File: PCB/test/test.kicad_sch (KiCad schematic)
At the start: 56 parts, among them CN4 HEADER_1X4, CN5 UFL, SW2 MLL1200S_TE, U1 STM32WBxx_QFN48, U2 USBLC6-2SC6, U3 LD3985M33R, X1 NX2016_32MHz, X2 NX2012_32K768Hz

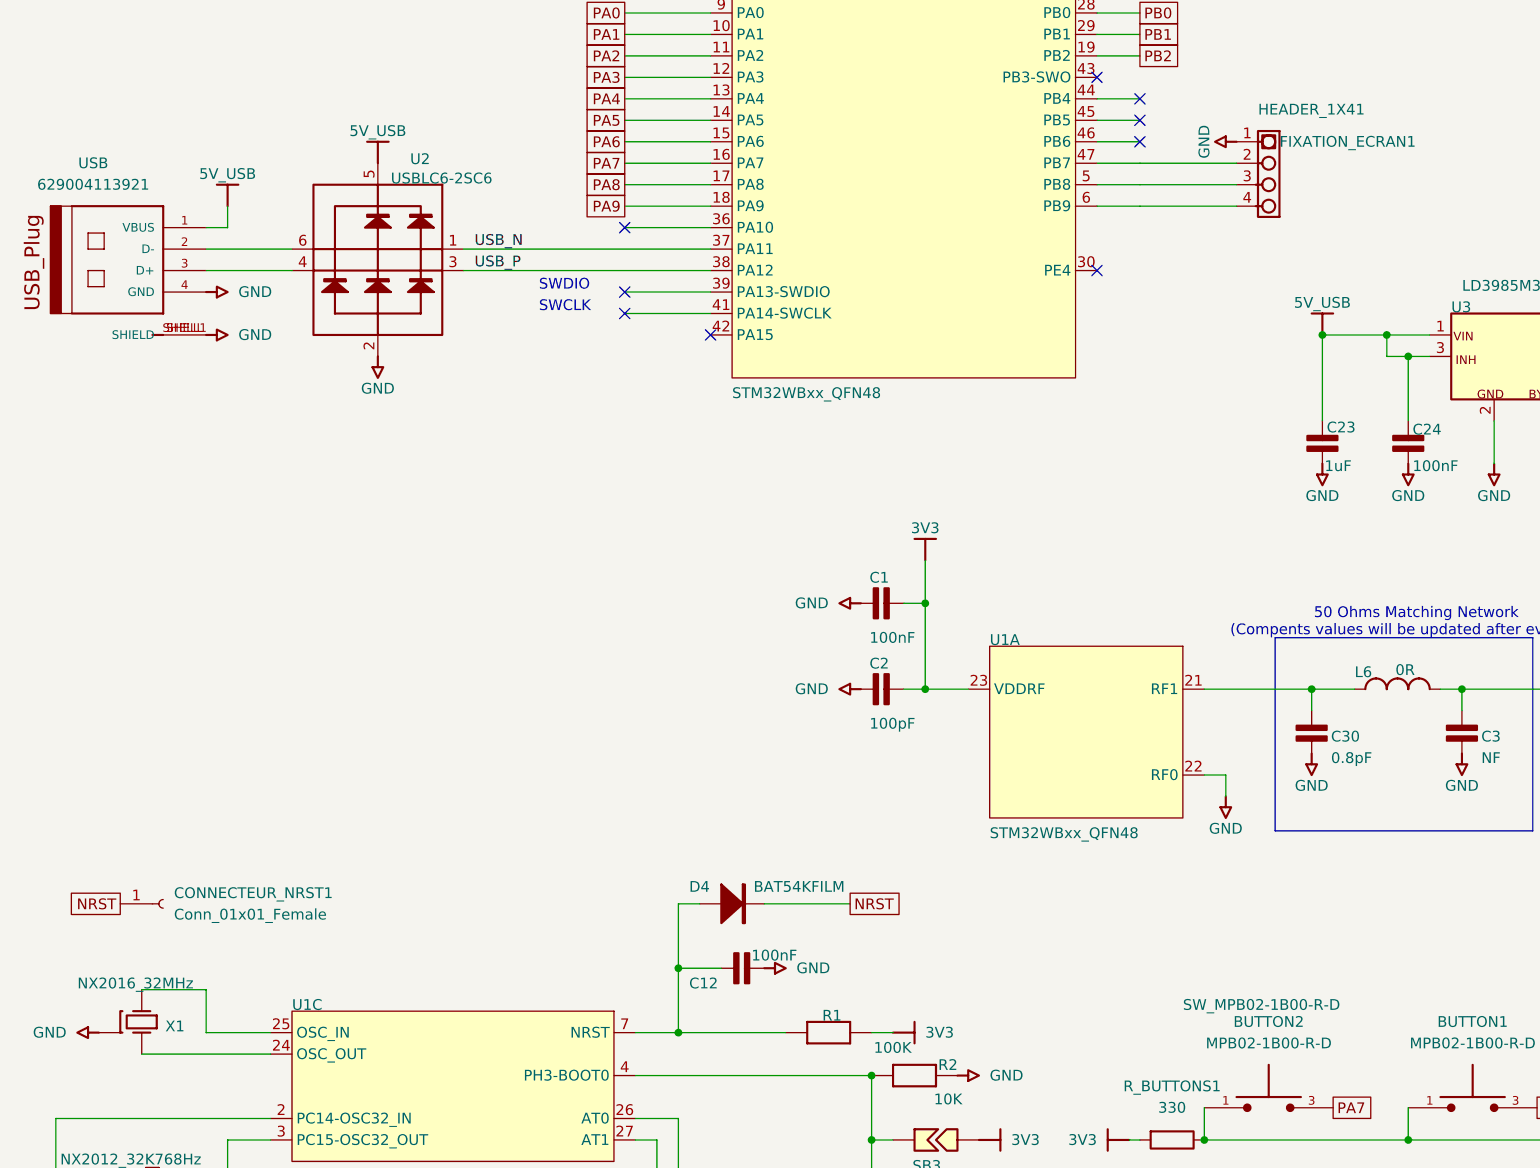
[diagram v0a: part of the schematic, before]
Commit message: ajout de l'usb dans le pcb
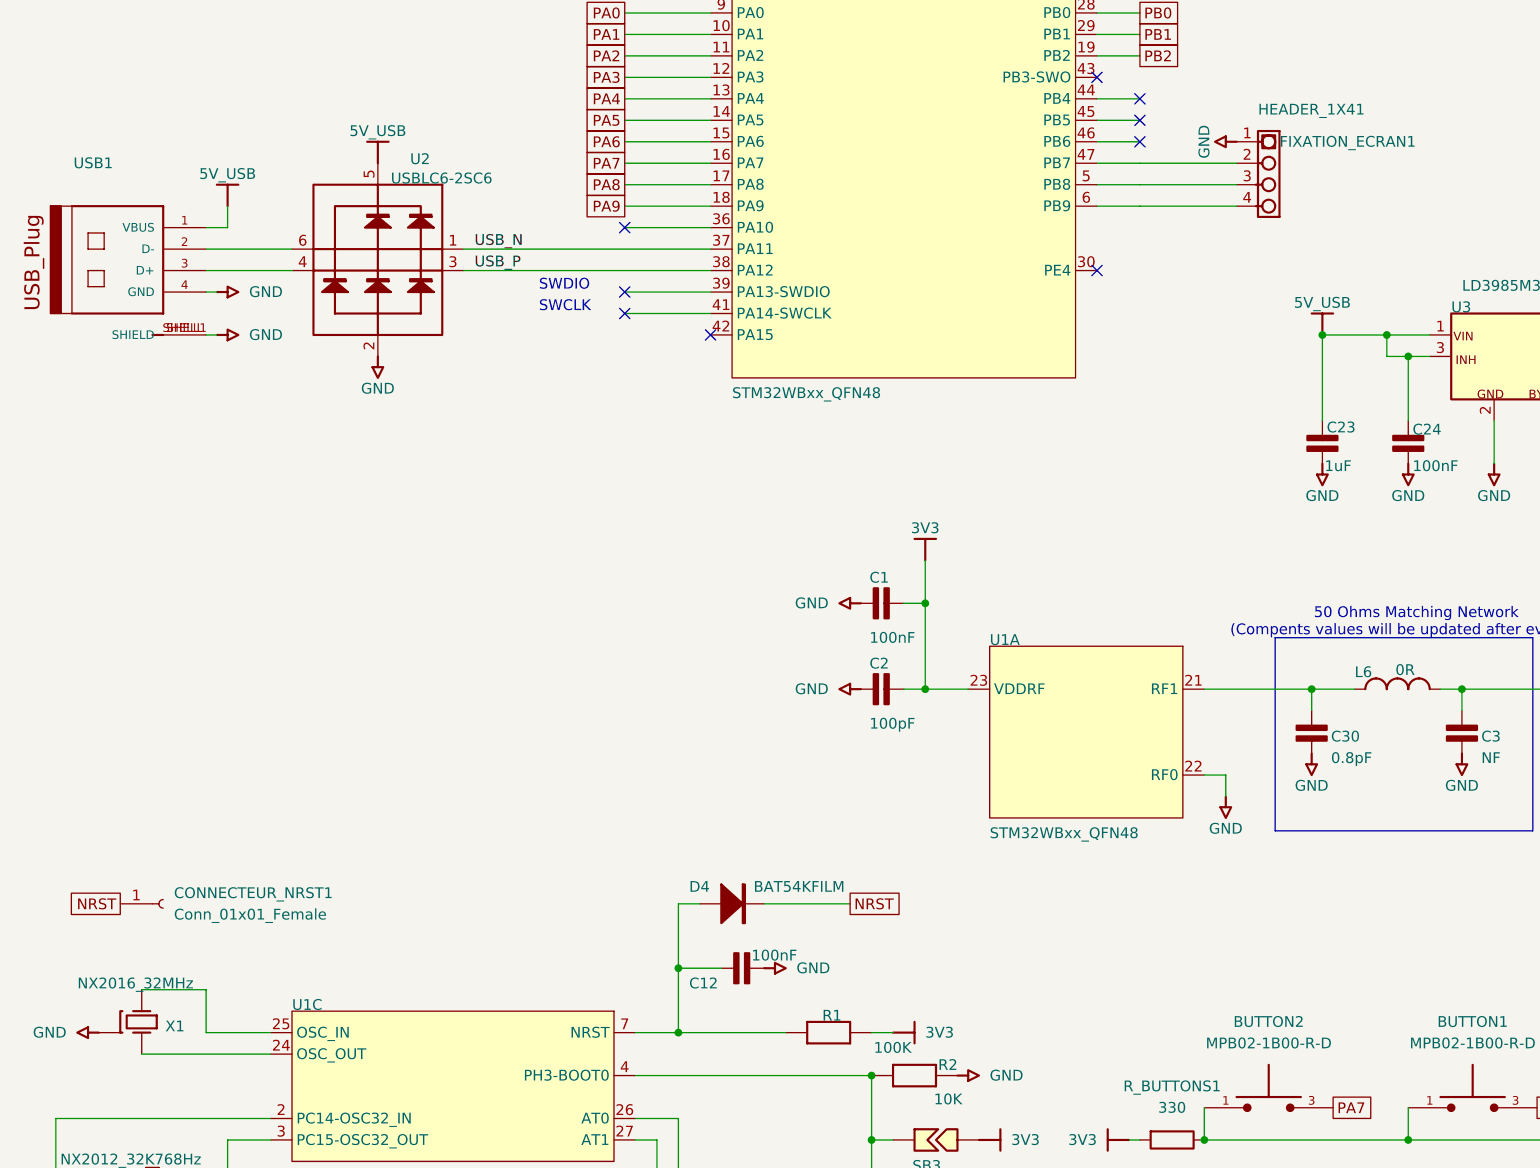
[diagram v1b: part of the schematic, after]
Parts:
- BUTTON1, BUTTON2, BUTTON3: footprint SW_MPB02-1B00-R-D -> (none)
- BUZZER1: footprint CUI_CMT-4023S-SMT-TR -> (none)
- C1, C10, C12, C15, C16, C17, C18, C19, C2, C20, C21, C22, C24, C25, C27, C28, C29, C3, C30, C4, C6, C7, C8, C9: footprint 0402_CAP_NPOL -> (none)
- C23, C26: footprint 0603_CAP_NPOL -> (none)
- CN4: footprint SIL4_127_B -> (none)
- CN5: footprint UFL -> (none)
- D4: footprint SOD523 -> (none)
- FLT1: footprint LFB182G45CGFD436 -> (none)
- L1, L4, L6: footprint 0402_COIL -> (none)
- L2: footprint 0805_COIL -> (none)
- L3: footprint 0603_COIL -> (none)
- OXYMETER1: footprint XDCR_SFH_7060 -> (none)
- R1, R2: footprint 0402_RES -> (none)
- SB1, SB3, SB4, SB5: footprint SB-tiny -> (none)
- SW2: footprint MLL1200S_TE -> (none)
- U1: footprint STM32WBxx_QFN48 -> (none)
- U2: footprint SOT23-6 -> (none)
- U3: footprint SOT23-5 -> (none)
- USB1: renamed from USB; value 629004113921 -> (none); footprint 629004113921 -> (none)
- X1: footprint NX2016_4P -> (none)
- X2: footprint NX2012_2P -> (none)

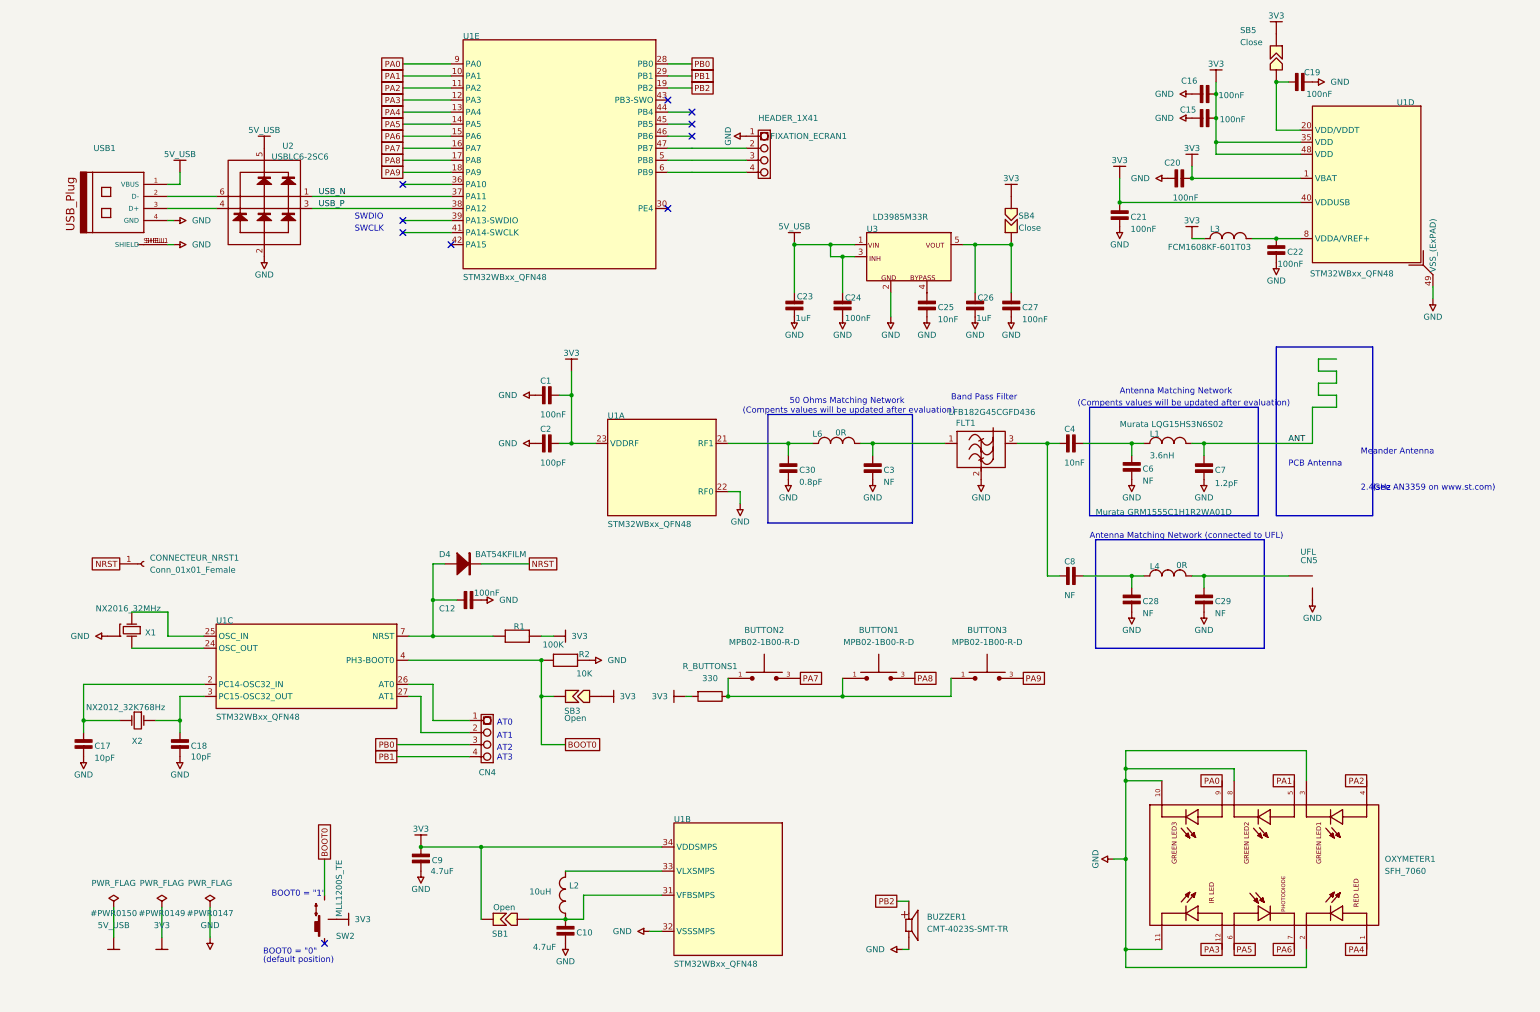
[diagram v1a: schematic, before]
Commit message: nouveaux boutons, réduction taille
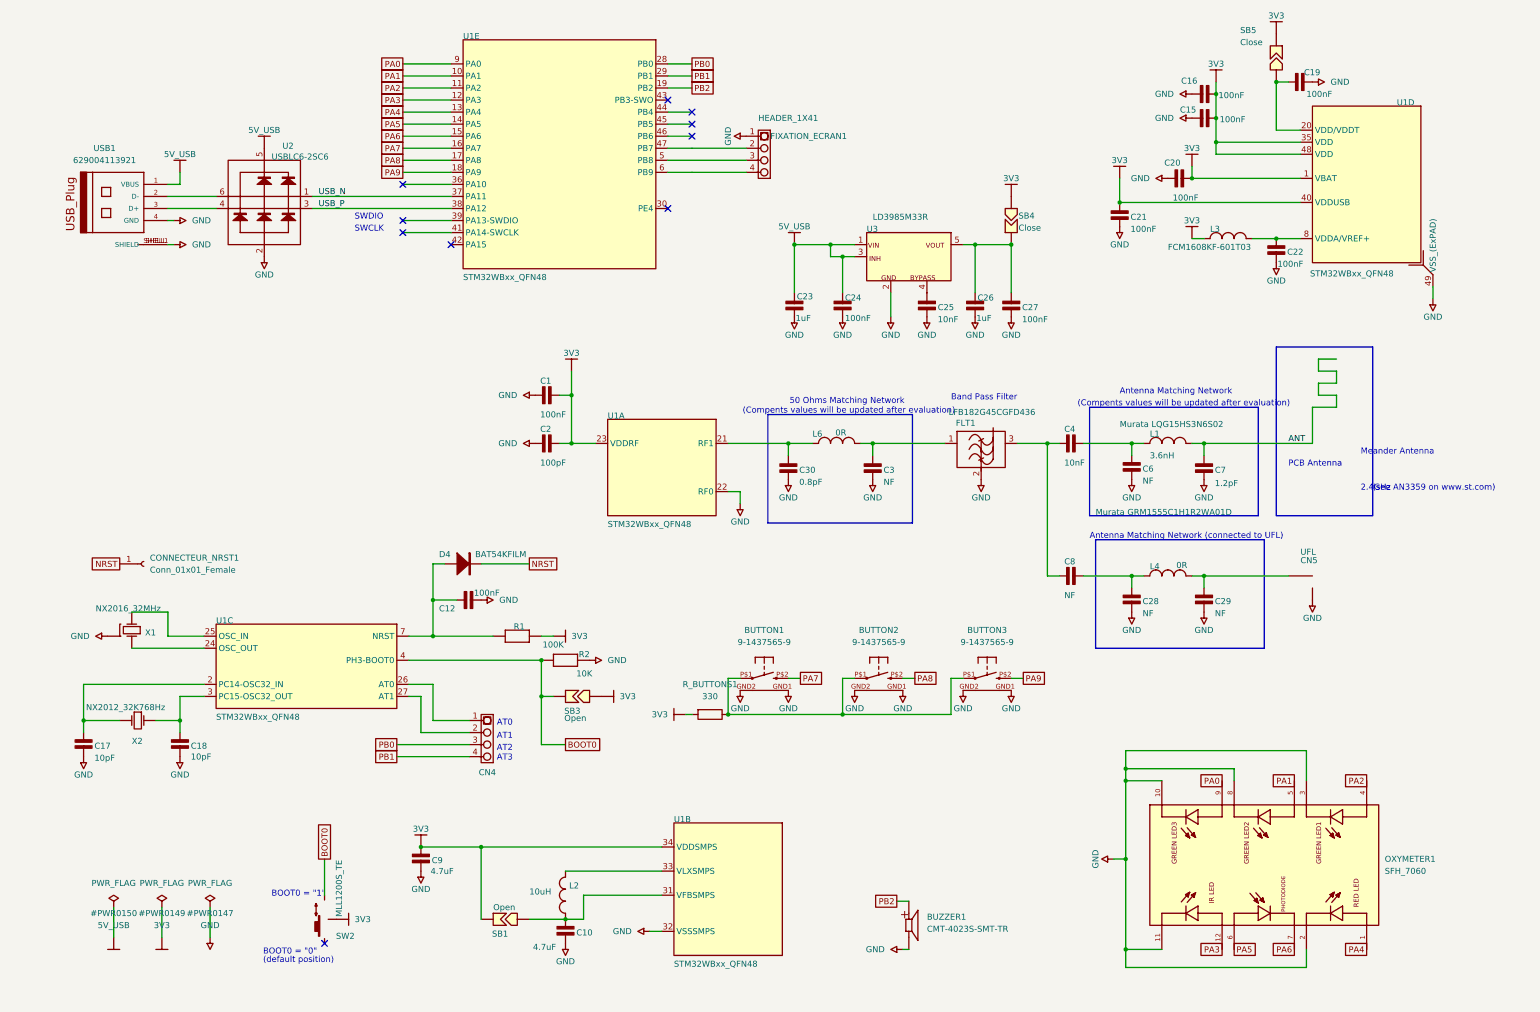
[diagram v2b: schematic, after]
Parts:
- removed BUTTON1, BUTTON2, BUTTON3: MPB02-1B00-R-D, symbol MPB02-1B00-R-D:MPB02-1B00-R-D
- added BUTTON1, BUTTON2, BUTTON3: 9-1437565-9, FSMRACD, symbol 9-1437565-9:9-1437565-9
- BUZZER1: footprint (none) -> CMT-4023S-SMT-TR:CUI_CMT-4023S-SMT-TR
- C1, C10, C12, C15, C16, C17, C18, C19, C2, C20, C21, C22, C24, C25, C27, C28, C29, C3, C30, C4, C6, C7, C8, C9: footprint (none) -> Library:0402_CAP_NPOL
- C23, C26: footprint (none) -> Library:0603_CAP_NPOL
- CN4: footprint (none) -> Library:SIL4_127_B
- CN5: footprint (none) -> Library:UFL
- D4: footprint (none) -> Library:SOD523
- FLT1: footprint (none) -> Library:LFB182G45CGFD436
- L1, L4, L6: footprint (none) -> Library:0402_COIL
- L2: footprint (none) -> Library:0805_COIL
- L3: footprint (none) -> Library:0603_COIL
- OXYMETER1: footprint (none) -> SFH_7060:XDCR_SFH_7060
- R1, R2: footprint (none) -> Library:0402_RES
- SB1, SB3, SB4, SB5: footprint (none) -> Library:SB-tiny
- SW2: footprint (none) -> Library:MLL1200S_TE
- U1: footprint (none) -> Library:STM32WBxx_QFN48
- U2: footprint (none) -> Library:SOT23-6
- U3: footprint (none) -> Library:SOT23-5
- USB1: value (none) -> 629004113921
- X1: footprint (none) -> Library:NX2016_4P
- X2: footprint (none) -> Library:NX2012_2P
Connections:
- net GND: now also BUTTON1.GND1, BUTTON1.GND2, BUTTON2.GND1, BUTTON2.GND2, BUTTON3.GND1, BUTTON3.GND2
- net PA7: now also BUTTON1.P$2
- net PA8: now also BUTTON2.P$2
- net PA9: now also BUTTON3.P$2
- net at R_BUTTONS1.1: now also BUTTON1.P$1, BUTTON2.P$1, BUTTON3.P$1
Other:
- moved on the sheet: R_BUTTONS1

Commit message: réduction taille des routes
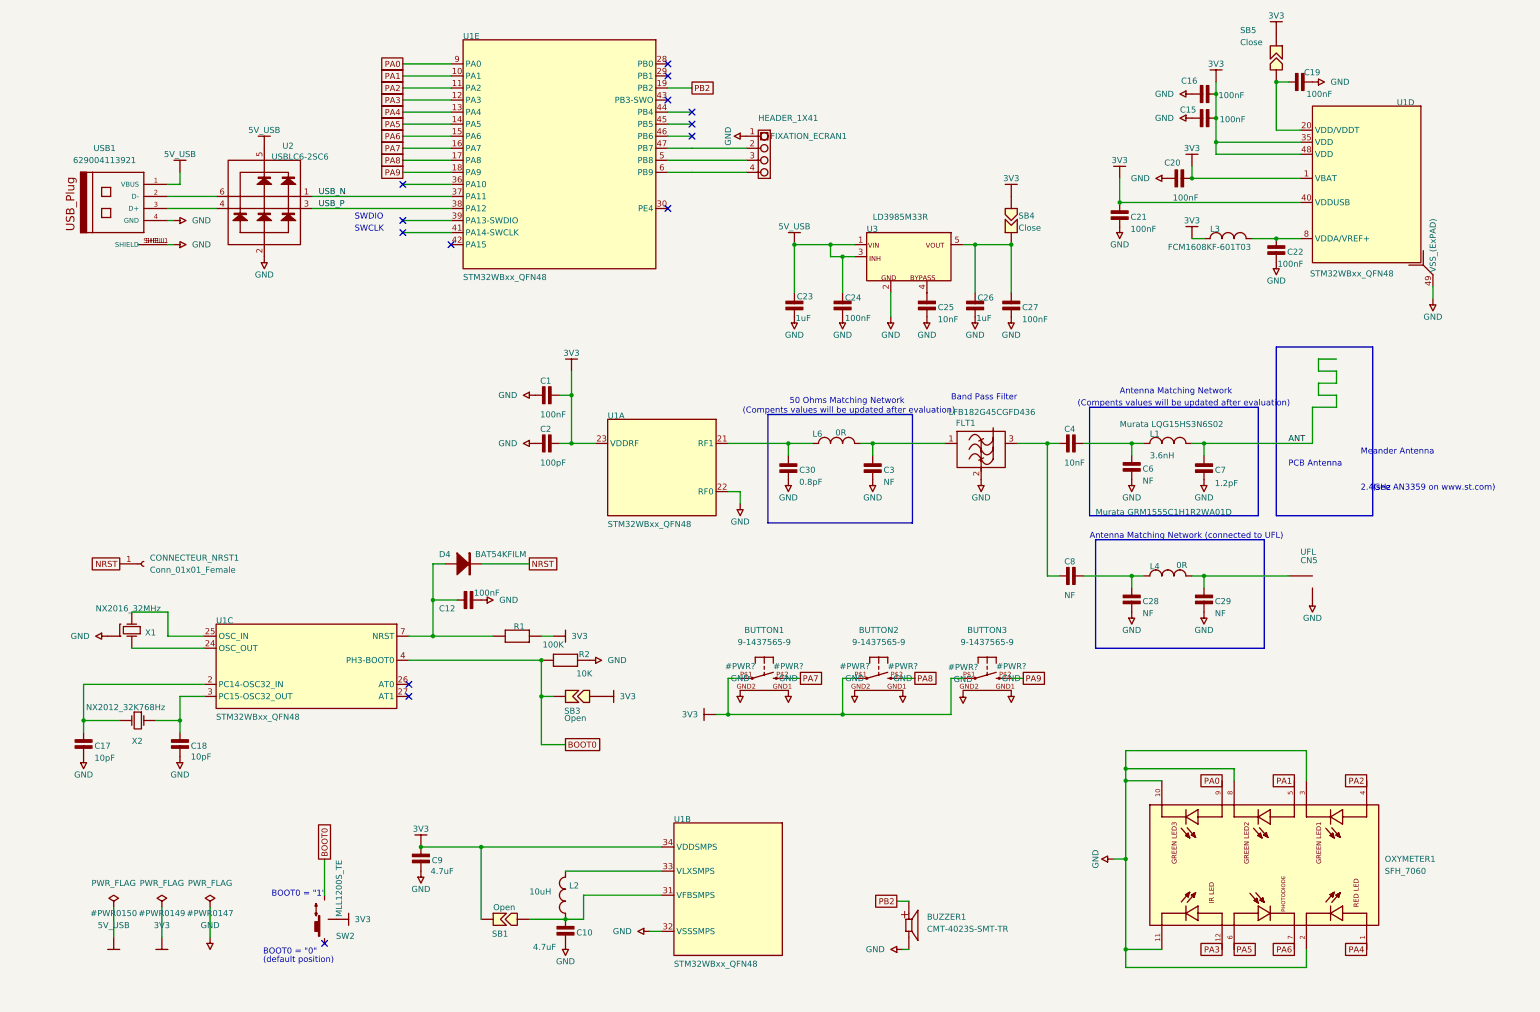
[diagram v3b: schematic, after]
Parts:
- removed CN4: HEADER_1X4, Library:SIL4_127_B, symbol test-altium-import:0_mirrored_HEADER_1X4
- removed R_BUTTONS1: 330, Resistor_SMD:R_0402_1005Metric, symbol Device:R
- USB1: footprint (none) -> 629004113921:629004113921
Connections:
- net 3V3: now also BUTTON1.P$1, BUTTON2.P$1, BUTTON3.P$1
- net GND: no longer BUTTON3.GND2
- net PB0: no longer names the net of U1.28 (PB0)
- net PB1: no longer names the net of U1.29 (PB1)
- no-connect marks 10 -> 14
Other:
- note removed: "AT0"
- note removed: "AT1"
- note removed: "AT2"
- note removed: "AT3"

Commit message: small error fixes
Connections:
- net GND: now also BUTTON3.GND2
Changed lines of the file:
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@@
     (pin "")
   )
-  (symbol (lib_id "test-altium-import:GND") (at 190.5 144.9656 0) (unit 1)
+  (symbol (lib_id "test-altium-import:GND") (at 190.5 144.78 0) (unit 1)
     (in_bom yes) (on_board yes) (fields_autoplaced)
-    (property "Reference" "#PWR?" (id 0) (at 190.5 139.8856 0))
-    (property "Value" "GND" (id 1) (at 190.5 142.4256 0))
-    (property "Footprint" "" (id 2) (at 190.5 144.9656 0)
+    (property "Reference" "#PWR?" (id 0) (at 190.5 139.7 0))
+    (property "Value" "GND" (id 1) (at 190.5 142.24 0))
+    (property "Footprint" "" (id 2) (at 190.5 144.78 0)
       (effects (font (size 1.27 1.27)) hide)
     )
-    (property "Datasheet" "" (id 3) (at 190.5 144.9656 0)
+    (property "Datasheet" "" (id 3) (at 190.5 144.78 0)
       (effects (font (size 1.27 1.27)) hide)
     )
